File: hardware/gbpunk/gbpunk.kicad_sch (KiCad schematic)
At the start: 48 parts, among them J1 CART, J4 SWD_CONNECTOR, P1 USB_C_CONNECTOR, SW7 RESET, SW9 USB_BOOT, U1 RP2040, U2 SN74LVC4245A, U3 W25Q128JVS, U4 NCP1117-3.3_SOT223, U5 SN74LVC4245A, U6 SN74LVC4245A, U7 SN74LVC4245A, Y1 12MHz

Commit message: gotta swap all the pins now :(
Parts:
- added J2: SWD_CONNECTOR, Connector_PinHeader_2.54mm:PinHeader_1x05_P2.54mm_Vertical, symbol Connector_Generic:Conn_01x05
- added JP1, JP3, JP4: SWDIR_1, Jumper:SolderJumper-3_P1.3mm_Bridged12_RoundedPad1.0x1.5mm, symbol Jumper:Jumper_3_Bridged12
- added JP2: SWDIR_0, Jumper:SolderJumper-3_P1.3mm_Bridged12_RoundedPad1.0x1.5mm, symbol Jumper:Jumper_3_Bridged12
- added R15: 56k, Resistor_SMD:R_0402_1005Metric_Pad0.72x0.64mm_HandSolder, symbol Device:R
- added TP1: 1V1_TP, TestPoint:TestPoint_Pad_D1.0mm, symbol Connector:TestPoint
- added TP2: RUN_TP, TestPoint:TestPoint_Pad_D1.0mm, symbol Connector:TestPoint
- added TP3: 3V3_TP, TestPoint:TestPoint_Pad_D1.0mm, symbol Connector:TestPoint
- added TP4: DBUS_DIR_TP, TestPoint:TestPoint_Pad_D1.0mm, symbol Connector:TestPoint
- added TP5: 5V0_TP, TestPoint:TestPoint_Pad_D1.0mm, symbol Connector:TestPoint
- J1: footprint gbpunk:GameBoy_Cartridge_1x32_P1.50mm_Edge -> gbpunk:gbpunk_aliexpress_gb_connector
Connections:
- net +1V1: now also TP1.1
- net +3.3V: now also J2.5 (Pin_5), TP3.1
- net +5V: now also JP2.3 (B), JP3.3 (B), JP4.3 (B), TP5.1; no longer R1.2, R4.2, R6.2
- net GND: now also J2.4 (Pin_4), JP2.2 (C), JP3.2 (C), JP4.2 (C), R15.2
- net RUN: now also J2.3 (Pin_3), TP2.1
- net SWCLK: now also J2.2 (Pin_2)
- net SWDIO: now also J2.1 (Pin_1)
- net ~{RD}: now also JP1.3 (B); no longer U7.2 (DIR)
- net ~{WR}: now also JP1.2 (C)
- new net: JP4.1 (A), R6.2
- new net: JP1.1 (A), TP4.1, U7.2 (DIR)
- new net: JP2.1 (A), R1.2
- new net: JP3.1 (A), R4.2

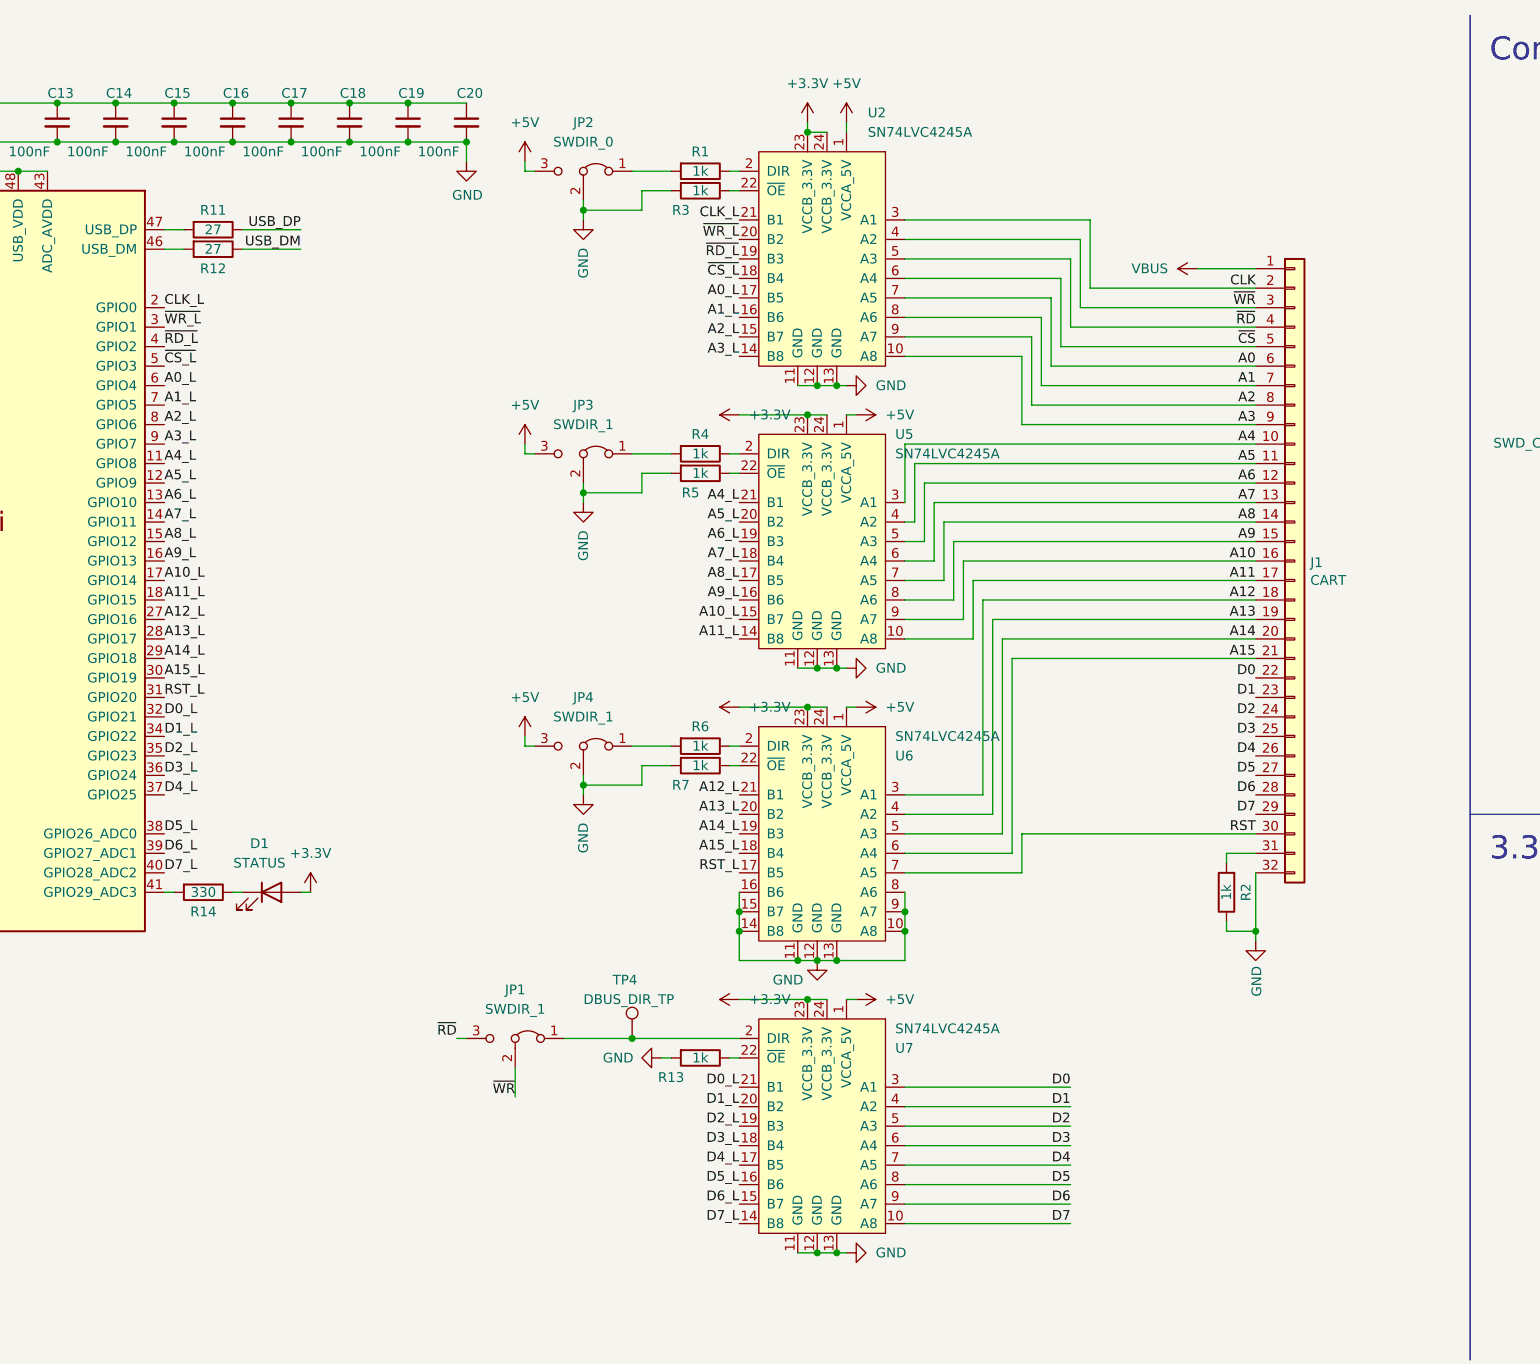
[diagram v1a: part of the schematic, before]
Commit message: big PCB reroute so the connector is not upside down
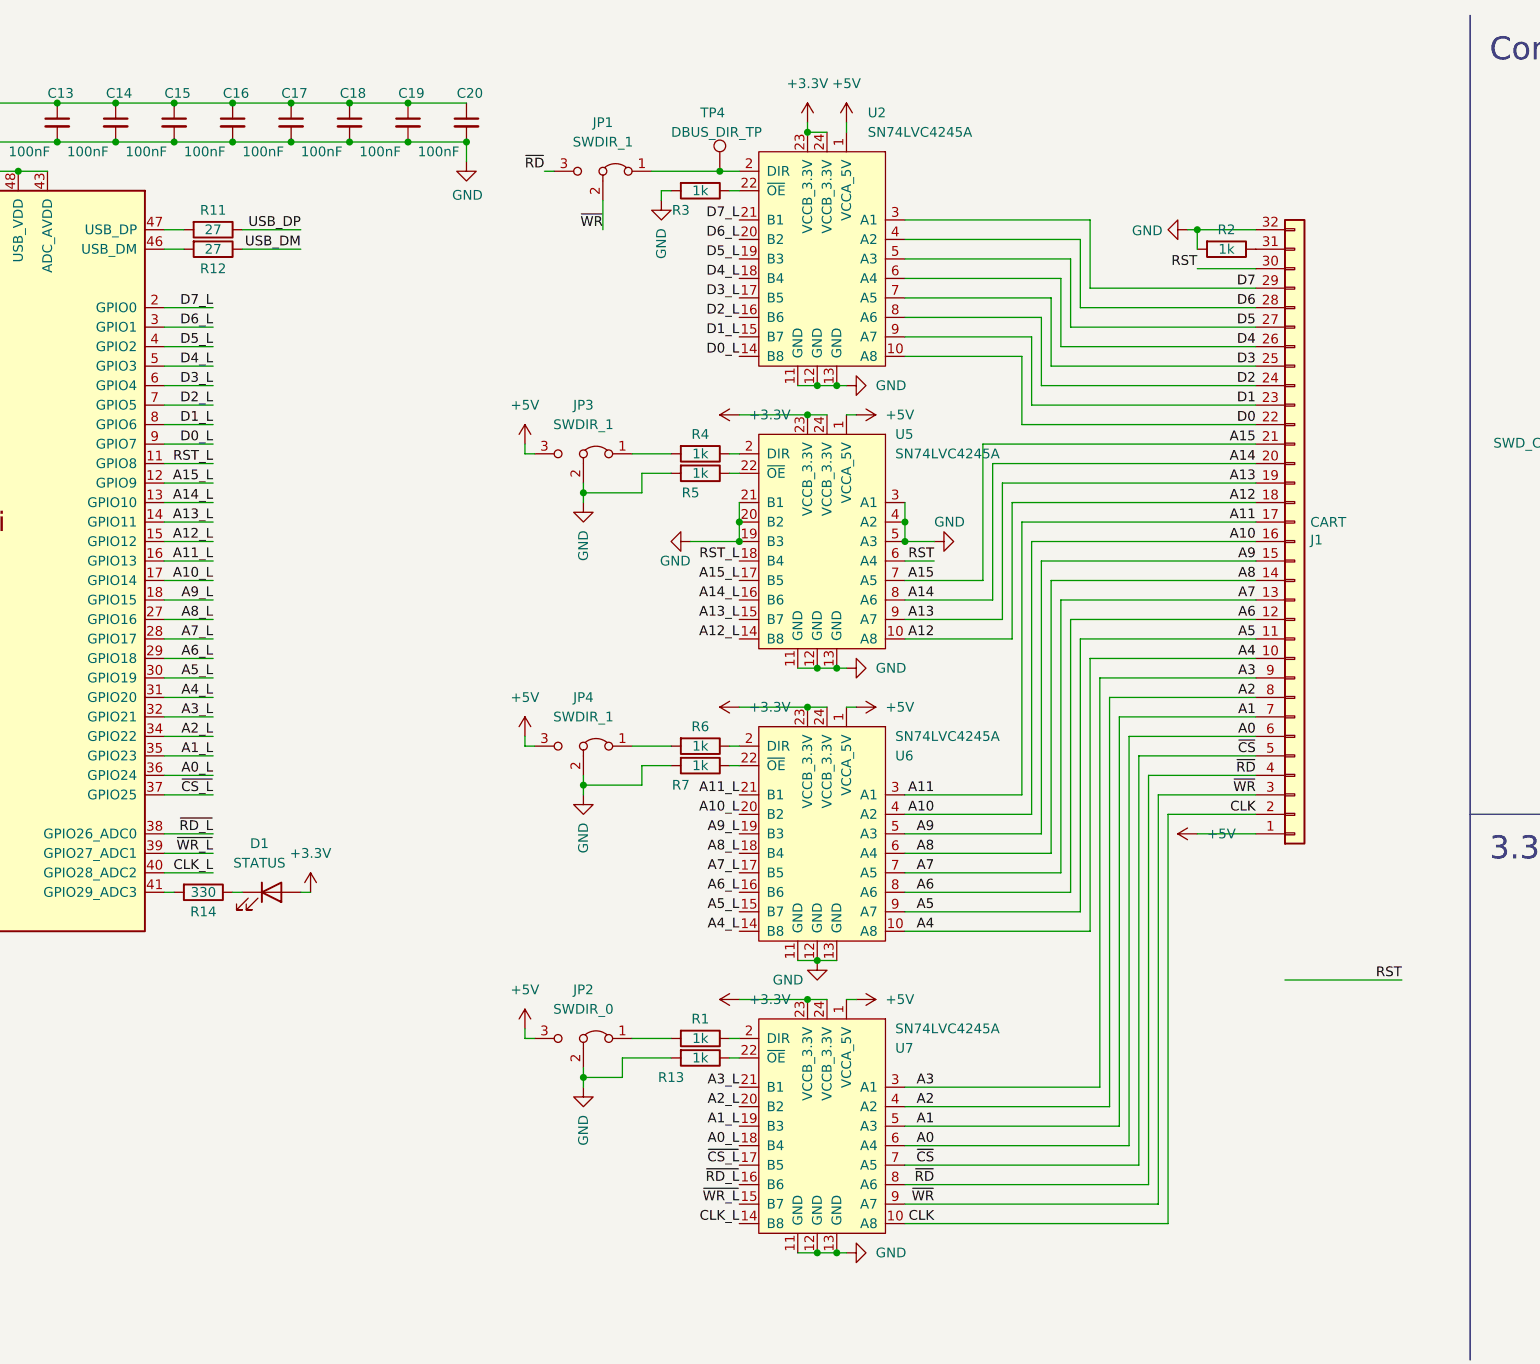
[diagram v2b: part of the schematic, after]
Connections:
- net +5V: now also J1.1 (Pin_1)
- net A0: now also U7.6 (A4); no longer U2.7 (A5)
- net A0_L: now also U1.36 (GPIO24), U7.18 (B4); no longer U1.6 (GPIO4), U2.17 (B5)
- net A1: now also U7.5 (A3); no longer U2.8 (A6)
- net A10: now also U6.4 (A2); no longer U5.9 (A7)
- net A10_L: now also U6.20 (B2); no longer U5.15 (B7)
- net A11: now also U6.3 (A1); no longer U5.10 (A8)
- net A11_L: now also U1.16 (GPIO13), U6.21 (B1); no longer U1.18 (GPIO15), U5.14 (B8)
- net A12: now also U5.10 (A8); no longer U6.3 (A1)
- net A12_L: now also U1.15 (GPIO12), U5.14 (B8); no longer U1.27 (GPIO16), U6.21 (B1)
- net A13: now also U5.9 (A7); no longer U6.4 (A2)
- net A13_L: now also U1.14 (GPIO11), U5.15 (B7); no longer U1.28 (GPIO17), U6.20 (B2)
- net A14: now also U5.8 (A6); no longer U6.5 (A3)
- net A14_L: now also U1.13 (GPIO10), U5.16 (B6); no longer U1.29 (GPIO18), U6.19 (B3)
- net A15: now also U5.7 (A5); no longer U6.6 (A4)
- net A15_L: now also U1.12 (GPIO9), U5.17 (B5); no longer U1.30 (GPIO19), U6.18 (B4)
- net A1_L: now also U1.35 (GPIO23), U7.19 (B3); no longer U1.7 (GPIO5), U2.16 (B6)
- net A2: now also U7.4 (A2); no longer U2.9 (A7)
- net A2_L: now also U1.34 (GPIO22), U7.20 (B2); no longer U1.8 (GPIO6), U2.15 (B7)
- net A3: now also U7.3 (A1); no longer U2.10 (A8)
- net A3_L: now also U1.32 (GPIO21), U7.21 (B1); no longer U1.9 (GPIO7), U2.14 (B8)
- net A4: now also U6.10 (A8); no longer U5.3 (A1)
- net A4_L: now also U1.31 (GPIO20), U6.14 (B8); no longer U1.11 (GPIO8), U5.21 (B1)
- net A5: now also U6.9 (A7); no longer U5.4 (A2)
- net A5_L: now also U1.30 (GPIO19), U6.15 (B7); no longer U1.12 (GPIO9), U5.20 (B2)
- net A6: now also U6.8 (A6); no longer U5.5 (A3)
- net A6_L: now also U1.29 (GPIO18), U6.16 (B6); no longer U1.13 (GPIO10), U5.19 (B3)
- net A7: now also U6.7 (A5); no longer U5.6 (A4)
- net A7_L: now also U1.28 (GPIO17), U6.17 (B5); no longer U1.14 (GPIO11), U5.18 (B4)
- net A8: now also U6.6 (A4); no longer U5.7 (A5)
- net A8_L: now also U1.27 (GPIO16), U6.18 (B4); no longer U1.15 (GPIO12), U5.17 (B5)
- net A9: now also U6.5 (A3); no longer U5.8 (A6)
- net A9_L: now also U1.18 (GPIO15), U6.19 (B3); no longer U1.16 (GPIO13), U5.16 (B6)
- net CLK: now also U7.10 (A8); no longer U2.3 (A1)
- net CLK_L: now also U1.40 (GPIO28_ADC2), U7.14 (B8); no longer U1.2 (GPIO0), U2.21 (B1)
- net D0: now also U2.10 (A8); no longer U7.3 (A1)
- net D0_L: now also U1.9 (GPIO7), U2.14 (B8); no longer U1.32 (GPIO21), U7.21 (B1)
- net D1: now also U2.9 (A7); no longer U7.4 (A2)
- net D1_L: now also U1.8 (GPIO6), U2.15 (B7); no longer U1.34 (GPIO22), U7.20 (B2)
- net D2: now also U2.8 (A6); no longer U7.5 (A3)
- net D2_L: now also U1.7 (GPIO5), U2.16 (B6); no longer U1.35 (GPIO23), U7.19 (B3)
- net D3: now also U2.7 (A5); no longer U7.6 (A4)
- net D3_L: now also U1.6 (GPIO4), U2.17 (B5); no longer U1.36 (GPIO24), U7.18 (B4)
- net D4: now also U2.6 (A4); no longer U7.7 (A5)
- net D4_L: now also U1.5 (GPIO3), U2.18 (B4); no longer U1.37 (GPIO25), U7.17 (B5)
- net D5: now also U2.5 (A3); no longer U7.8 (A6)
- net D5_L: now also U1.4 (GPIO2), U2.19 (B3); no longer U1.38 (GPIO26_ADC0), U7.16 (B6)
- net D6: now also U2.4 (A2); no longer U7.9 (A7)
- net D6_L: now also U1.3 (GPIO1), U2.20 (B2); no longer U1.39 (GPIO27_ADC1), U7.15 (B7)
- net D7: now also U2.3 (A1); no longer U7.10 (A8)
- net D7_L: now also U1.2 (GPIO0), U2.21 (B1); no longer U1.40 (GPIO28_ADC2), U7.14 (B8)
- net GND: now also R2.2, U5.19 (B3), U5.20 (B2), U5.21 (B1), U5.3 (A1), U5.4 (A2), U5.5 (A3); no longer R2.1, U6.10 (A8), U6.14 (B8), U6.15 (B7), U6.16 (B6), U6.8 (A6), U6.9 (A7)
- net RST: now also U5.6 (A4); no longer U6.7 (A5)
- net RST_L: now also U1.11 (GPIO8), U5.18 (B4); no longer U1.31 (GPIO20), U6.17 (B5)
- net VBUS: no longer J1.1 (Pin_1)
- net ~{CS_L}: now also U1.37 (GPIO25), U7.17 (B5); no longer U1.5 (GPIO3), U2.18 (B4)
- net ~{CS}: now also U7.7 (A5); no longer U2.6 (A4)
- net ~{RD_L}: now also U1.38 (GPIO26_ADC0), U7.16 (B6); no longer U1.4 (GPIO2), U2.19 (B3)
- net ~{RD}: now also U7.8 (A6); no longer U2.5 (A3)
- net ~{WR_L}: now also U1.39 (GPIO27_ADC1), U7.15 (B7); no longer U1.3 (GPIO1), U2.20 (B2)
- net ~{WR}: now also U7.9 (A7); no longer U2.4 (A2)
- net at J1.31 (Pin_31): now also R2.1; no longer R2.2
- net at JP1.1 (A), TP4.1: now also U2.2 (DIR); no longer U7.2 (DIR)
- net at R1.1: now also U7.2 (DIR); no longer U2.2 (DIR)
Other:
- moved on the sheet: JP1, JP2, R1, TP4

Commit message: orderd boards for V2
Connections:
- no-connect marks 13 -> 14
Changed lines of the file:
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@@
   (no_connect (at 342.9 72.39))
   (no_connect (at 400.05 73.66))
+  (no_connect (at 402.59 26.67))
   (no_connect (at 400.05 76.2))
   (no_connect (at 342.9 69.85))
